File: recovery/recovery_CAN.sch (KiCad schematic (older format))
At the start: 15 parts, among them J1 Conn_01x05_Female, U1 MCP2562, U2 PIC18F26K83, Y1 Crystal

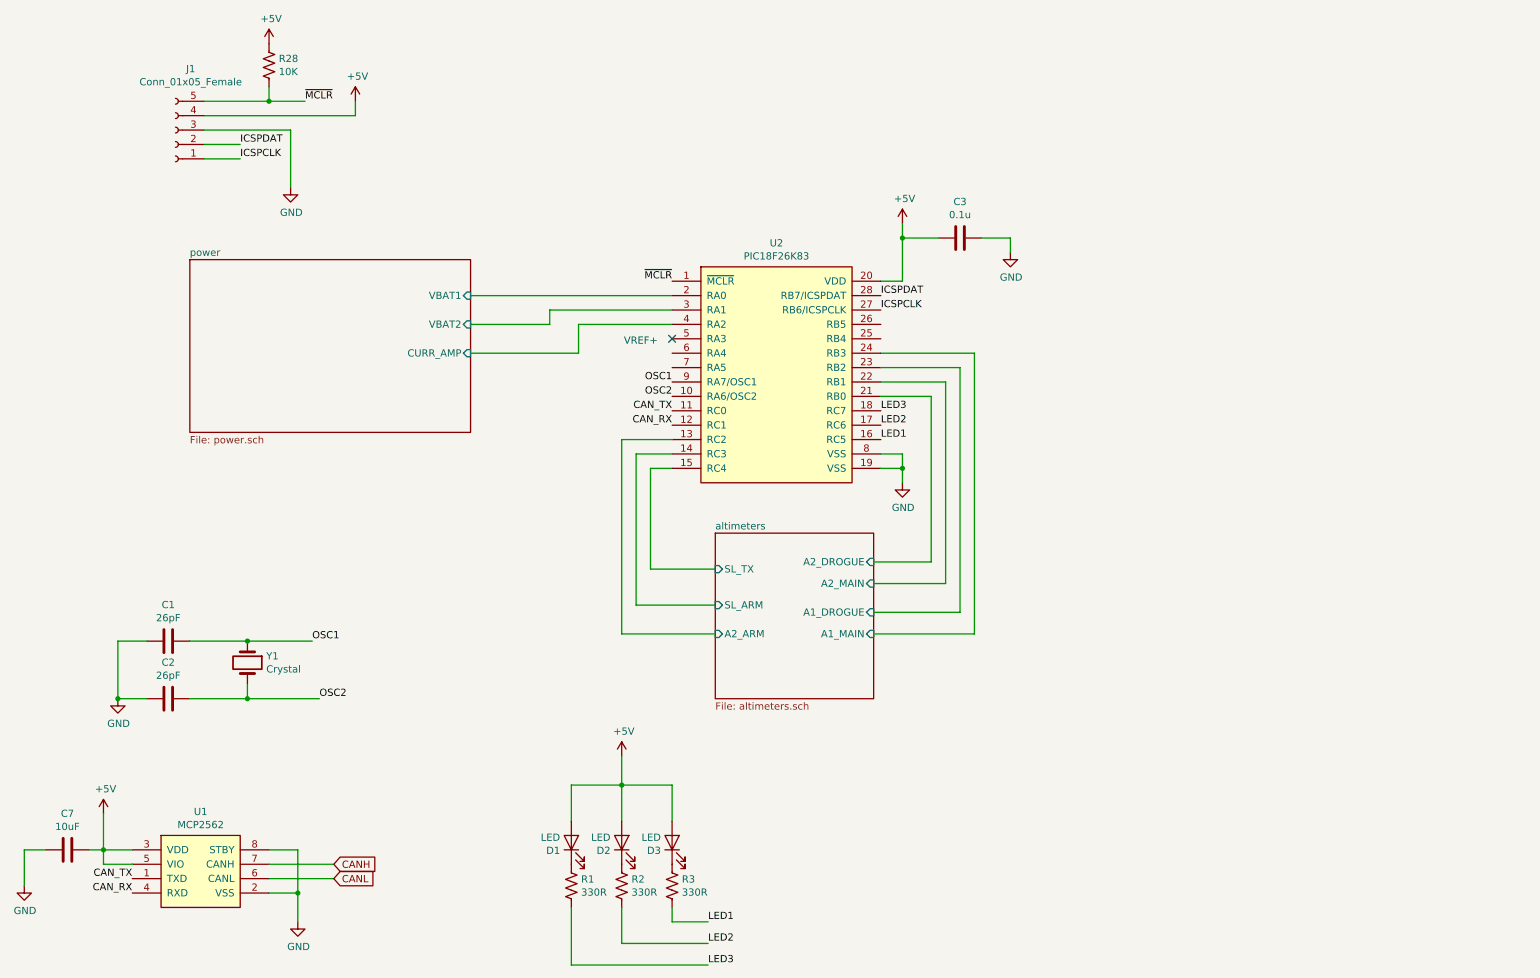
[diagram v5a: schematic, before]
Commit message: fix comments from scematic review, make mag switches powerup the PIC
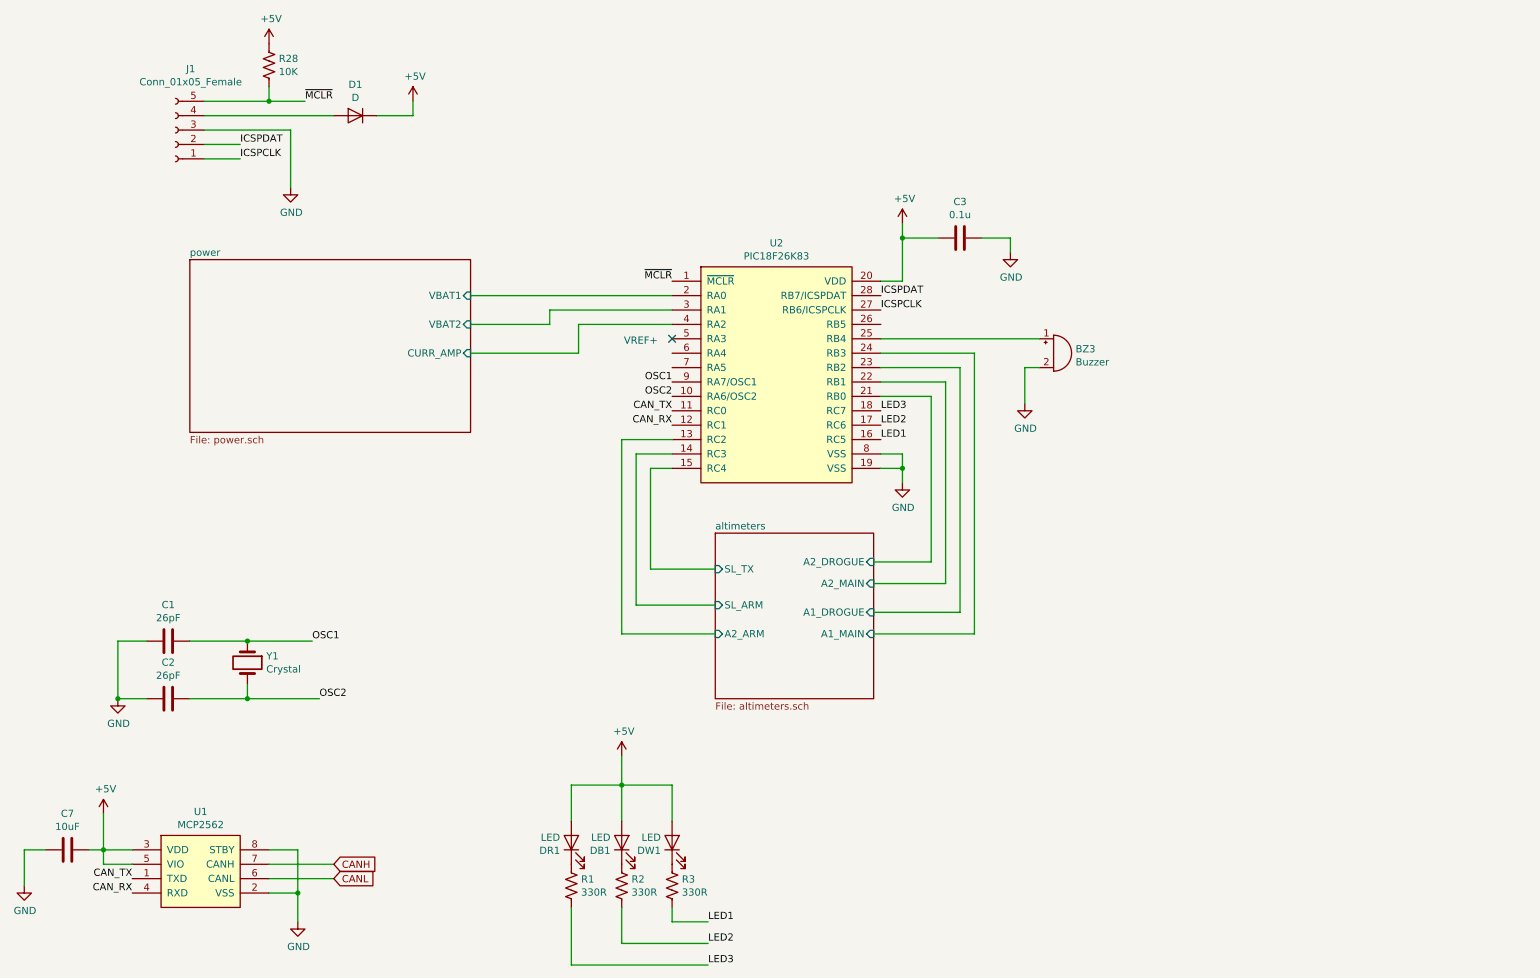
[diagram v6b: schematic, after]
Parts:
- added BZ3: Buzzer, symbol Device:Buzzer
- added D1: D, symbol Device:D
- renumbered D2 to DB1, D1 to DR1, D3 to DW1
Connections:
- net +5V: now also D1.1 (K); no longer J1.4 (Pin_4)
- net GND: now also BZ3.2 (+)
- net at U2.25 (RB4): now also BZ3.1 (-)
- new net: D1.2 (A), J1.4 (Pin_4)
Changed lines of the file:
@@
 L power:+5V #PWR03
 U 1 1 5D95A01E
-P 2950 1250
-F 0 "#PWR03" H 2950 1100 50  0001 C CNN
-F 1 "+5V" H 2965 1423 50  0000 C CNN
-F 2 "" H 2950 1250 50  0001 C CNN
-F 3 "" H 2950 1250 50  0001 C CNN
-	1    2950 1250
-	1    0    0    -1
-$EndComp
-Wire Wire Line
-	1900 1350 2950 1350
-Wire Wire Line
-	2950 1350 2950 1250
+P 3350 1250
+F 0 "#PWR03" H 3350 1100 50  0001 C CNN
+F 1 "+5V" H 3365 1423 50  0000 C CNN
+F 2 "" H 3350 1250 50  0001 C CNN
+F 3 "" H 3350 1250 50  0001 C CNN
+	1    3350 1250
+	1    0    0    -1
+$EndComp
+Wire Wire Line
+	1900 1350 2800 1350
 $Comp
 L power:GND #PWR04
@@
 $EndSheet
 $Comp
-L Device:LED D3
+L Device:LED DW1
 U 1 1 5DAA8959
 P 5150 6400
-F 0 "D3" V 5095 6478 50  0000 L CNN
+F 0 "DW1" V 5095 6478 50  0000 L CNN
 F 1 "LED" V 5186 6478 50  0000 L CNN
 F 2 "" H 5150 6400 50  0001 C CNN
@@
 $EndComp
 $Comp
-L Device:LED D2
+L Device:LED DB1
 U 1 1 5DAA89D1
 P 4800 6400
-F 0 "D2" V 4745 6478 50  0000 L CNN
+F 0 "DB1" V 4745 6478 50  0000 L CNN
 F 1 "LED" V 4836 6478 50  0000 L CNN
 F 2 "" H 4800 6400 50  0001 C CNN
@@
 $EndComp
 $Comp
-L Device:LED D1
+L Device:LED DR1
 U 1 1 5DAA8A2E
 P 4450 6400
-F 0 "D1" V 4395 6478 50  0000 L CNN
+F 0 "DR1" V 4395 6478 50  0000 L CNN
 F 1 "LED" V 4486 6478 50  0000 L CNN
 F 2 "" H 4450 6400 50  0001 C CNN
@@
 Wire Wire Line
 	1400 6550 1200 6550
-Wire Wire Line
-	1200 6200 1200 6450
 Connection ~ 1200 6450
 Wire Wire Line
@@
 	2200 5000 2650 5000
 Connection ~ 2200 5000
+Wire Wire Line
+	1200 6200 1200 6450
+$Comp
+L Device:D D1
+U 1 1 5DC3AC48
+P 2950 1350
+F 0 "D1" H 2950 1566 50  0000 C CNN
+F 1 "D" H 2950 1475 50  0000 C CNN
+F 2 "" H 2950 1350 50  0001 C CNN
+F 3 "~" H 2950 1350 50  0001 C CNN
+	1    2950 1350
+	-1   0    0    -1
+$EndComp
+Wire Wire Line
+	3350 1250 3350 1350
+Wire Wire Line
+	3350 1350 3100 1350
+$Comp
+L Device:Buzzer BZ3
+U 1 1 5DC989E9
+P 7800 3000
+F 0 "BZ3" H 7953 3029 50  0000 L CNN
+F 1 "Buzzer" H 7953 2938 50  0000 L CNN
+F 2 "" V 7775 3100 50  0001 C CNN
+F 3 "~" V 7775 3100 50  0001 C CNN
+	1    7800 3000
+	1    0    0    -1
+$EndComp
+Wire Wire Line
+	6600 2900 7700 2900
+$Comp
+L power:GND #PWR010
+U 1 1 5DC9A870
+P 7600 3350
+F 0 "#PWR010" H 7600 3100 50  0001 C CNN
+F 1 "GND" H 7605 3177 50  0000 C CNN
+F 2 "" H 7600 3350 50  0001 C CNN
+F 3 "" H 7600 3350 50  0001 C CNN
+	1    7600 3350
+	1    0    0    -1
+$EndComp
+Wire Wire Line
+	7700 3100 7600 3100
+Wire Wire Line
+	7600 3100 7600 3350
 $EndSCHEMATC

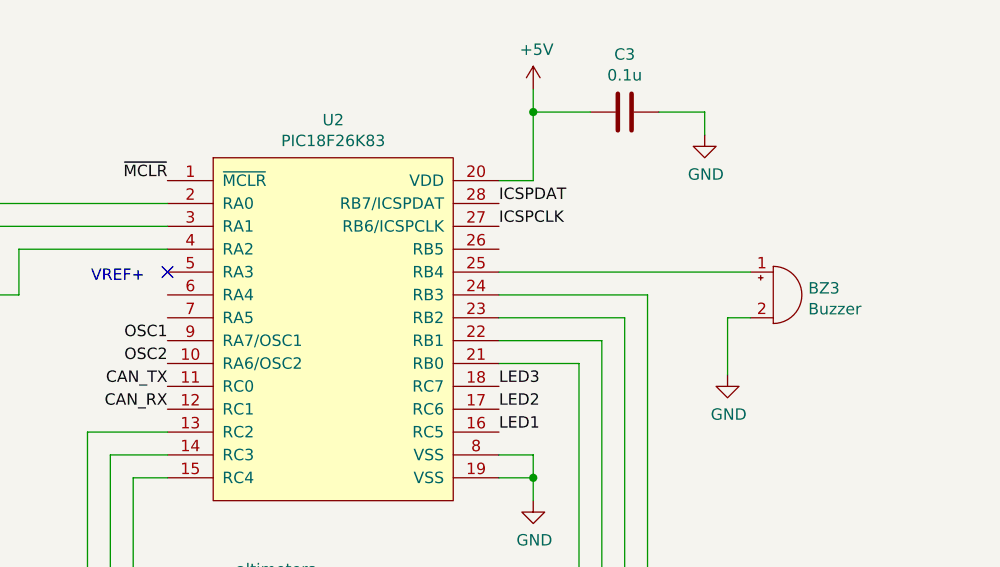
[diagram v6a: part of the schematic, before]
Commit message: add part numbers for buzzers
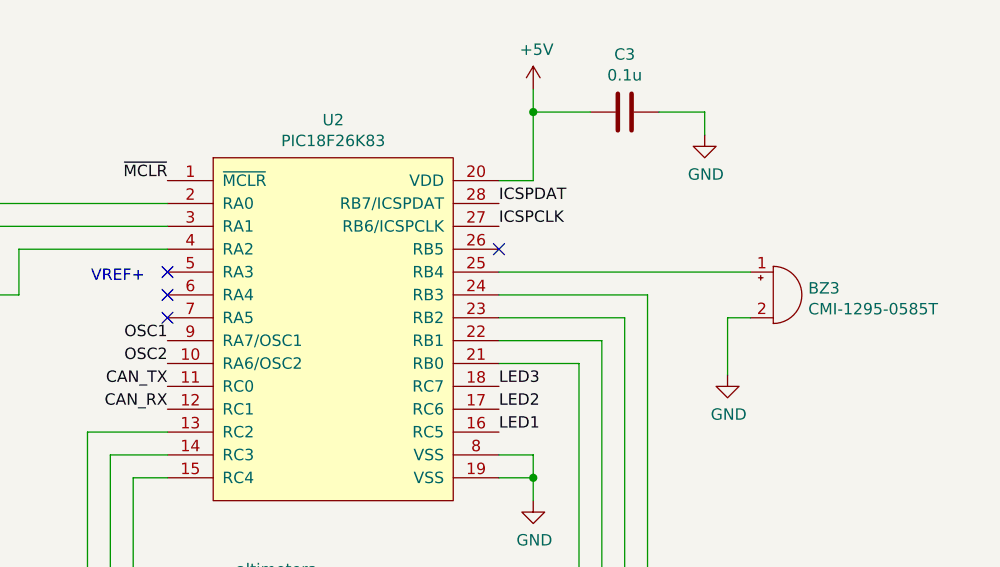
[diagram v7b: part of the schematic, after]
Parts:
- BZ3: value Buzzer -> CMI-1295-0585T
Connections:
- no-connect marks 1 -> 4
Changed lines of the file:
@@
 P 7800 3000
 F 0 "BZ3" H 7953 3029 50  0000 L CNN
-F 1 "Buzzer" H 7953 2938 50  0000 L CNN
+F 1 "CMI-1295-0585T" H 7953 2938 50  0000 L CNN
 F 2 "" V 7775 3100 50  0001 C CNN
 F 3 "~" V 7775 3100 50  0001 C CNN
@@
 Wire Wire Line
 	7600 3100 7600 3350
+NoConn ~ 6600 2800
+NoConn ~ 5150 3000
+NoConn ~ 5150 3100
 $EndSCHEMATC

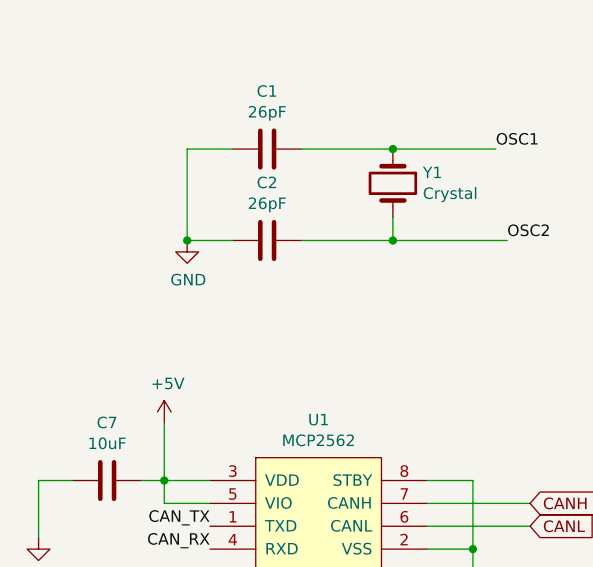
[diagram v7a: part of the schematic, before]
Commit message: Redesined scematic to reflect change to conectors for altimeter wiring, added more solder jumpers for increased board flexibility, created PCB file.
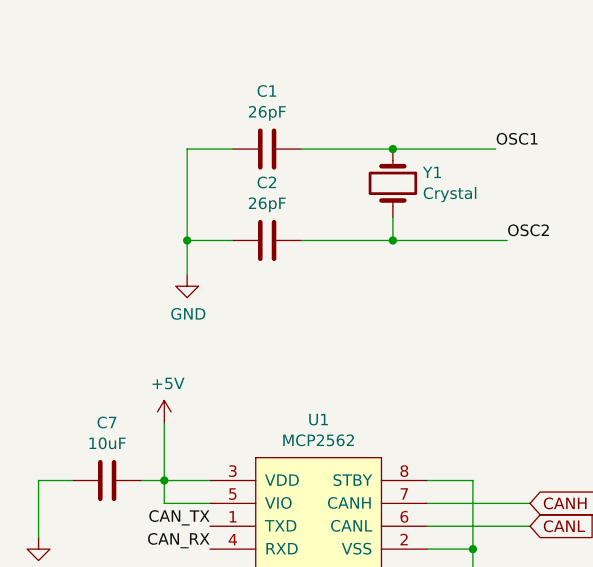
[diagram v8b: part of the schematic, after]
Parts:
- C1, C2, C3, C7: footprint (none) -> Capacitor_SMD:C_0805_2012Metric_Pad1.15x1.40mm_HandSolder
- DB1, DR1, DW1: footprint (none) -> LED_SMD:LED_1206_3216Metric_Pad1.42x1.75mm_HandSolder
- J1: footprint (none) -> canhw_footprints:PinHeader_5x2.54_SMD_90deg_952-3198-1-ND
- R1, R2, R28, R3: footprint (none) -> Resistor_SMD:R_0805_2012Metric_Pad1.15x1.40mm_HandSolder
- U1: footprint (none) -> Package_SO:SOIC-8_3.9x4.9mm_P1.27mm
- U2: footprint (none) -> Package_SO:SOIC-28W_7.5x18.7mm_P1.27mm
- Y1: footprint (none) -> Crystal:Crystal_HC49-4H_Vertical
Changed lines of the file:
@@
 F 0 "U2" H 5875 4065 50  0000 C CNN
 F 1 "PIC18F26K83" H 5875 3974 50  0000 C CNN
-F 2 "" H 6350 3150 50  0001 C CNN
+F 2 "Package_SO:SOIC-28W_7.5x18.7mm_P1.27mm" H 6350 3150 50  0001 C CNN
 F 3 "http://ww1.microchip.com/downloads/en/DeviceDoc/40001943A.pdf" H 6350 3150 50  0001 C CNN
 	1    5900 3150
@@
 F 0 "C3" V 6898 2200 50  0000 C CNN
 F 1 "0.1u" V 6989 2200 50  0000 C CNN
-F 2 "" H 7188 2050 50  0001 C CNN
+F 2 "Capacitor_SMD:C_0805_2012Metric_Pad1.15x1.40mm_HandSolder" H 7188 2050 50  0001 C CNN
 F 3 "~" H 7150 2200 50  0001 C CNN
 	1    7150 2200
@@
 F 0 "Y1" V 2154 5281 50  0000 L CNN
 F 1 "Crystal" V 2245 5281 50  0000 L CNN
-F 2 "" H 2200 5150 50  0001 C CNN
+F 2 "Crystal:Crystal_HC49-4H_Vertical" H 2200 5150 50  0001 C CNN
 F 3 "~" H 2200 5150 50  0001 C CNN
 	1    2200 5150
@@
 F 0 "C1" V 1398 5000 50  0000 C CNN
 F 1 "26pF" V 1489 5000 50  0000 C CNN
-F 2 "" H 1688 4850 50  0001 C CNN
+F 2 "Capacitor_SMD:C_0805_2012Metric_Pad1.15x1.40mm_HandSolder" H 1688 4850 50  0001 C CNN
 F 3 "~" H 1650 5000 50  0001 C CNN
 	1    1650 5000
@@
 F 0 "C2" V 1398 5400 50  0000 C CNN
 F 1 "26pF" V 1489 5400 50  0000 C CNN
-F 2 "" H 1688 5250 50  0001 C CNN
+F 2 "Capacitor_SMD:C_0805_2012Metric_Pad1.15x1.40mm_HandSolder" H 1688 5250 50  0001 C CNN
 F 3 "~" H 1650 5400 50  0001 C CNN
 	1    1650 5400
@@
 L power:GND #PWR02
 U 1 1 5D8FD7A1
-P 1300 5400
-F 0 "#PWR02" H 1300 5150 50  0001 C CNN
-F 1 "GND" H 1305 5227 50  0000 C CNN
-F 2 "" H 1300 5400 50  0001 C CNN
-F 3 "" H 1300 5400 50  0001 C CNN
-	1    1300 5400
-	1    0    0    -1
-$EndComp
-Wire Wire Line
-	1500 5400 1300 5400
+P 1300 5550
+F 0 "#PWR02" H 1300 5300 50  0001 C CNN
+F 1 "GND" H 1305 5377 50  0000 C CNN
+F 2 "" H 1300 5550 50  0001 C CNN
+F 3 "" H 1300 5550 50  0001 C CNN
+	1    1300 5550
+	1    0    0    -1
+$EndComp
 Wire Wire Line
 	1500 5000 1300 5000
-Wire Wire Line
-	1300 5000 1300 5400
-Connection ~ 1300 5400
 Wire Wire Line
 	1800 5000 2200 5000
@@
 F 0 "J1" H 1594 1025 50  0000 C CNN
 F 1 "Conn_01x05_Female" H 1594 1116 50  0000 C CNN
-F 2 "" H 1700 1450 50  0001 C CNN
+F 2 "canhw_footprints:PinHeader_5x2.54_SMD_90deg_952-3198-1-ND" H 1700 1450 50  0001 C CNN
 F 3 "~" H 1700 1450 50  0001 C CNN
 	1    1700 1450
@@
 F 0 "DW1" V 5095 6478 50  0000 L CNN
 F 1 "LED" V 5186 6478 50  0000 L CNN
-F 2 "" H 5150 6400 50  0001 C CNN
+F 2 "LED_SMD:LED_1206_3216Metric_Pad1.42x1.75mm_HandSolder" H 5150 6400 50  0001 C CNN
 F 3 "~" H 5150 6400 50  0001 C CNN
 	1    5150 6400
@@
 F 0 "DB1" V 4745 6478 50  0000 L CNN
 F 1 "LED" V 4836 6478 50  0000 L CNN
-F 2 "" H 4800 6400 50  0001 C CNN
+F 2 "LED_SMD:LED_1206_3216Metric_Pad1.42x1.75mm_HandSolder" H 4800 6400 50  0001 C CNN
 F 3 "~" H 4800 6400 50  0001 C CNN
 	1    4800 6400
@@
 F 0 "DR1" V 4395 6478 50  0000 L CNN
 F 1 "LED" V 4486 6478 50  0000 L CNN
-F 2 "" H 4450 6400 50  0001 C CNN
+F 2 "LED_SMD:LED_1206_3216Metric_Pad1.42x1.75mm_HandSolder" H 4450 6400 50  0001 C CNN
 F 3 "~" H 4450 6400 50  0001 C CNN
 	1    4450 6400
@@
 F 0 "R3" H 5218 6746 50  0000 L CNN
 F 1 "330R" H 5218 6655 50  0000 L CNN
-F 2 "" V 5190 6690 50  0001 C CNN
+F 2 "Resistor_SMD:R_0805_2012Metric_Pad1.15x1.40mm_HandSolder" V 5190 6690 50  0001 C CNN
 F 3 "~" H 5150 6700 50  0001 C CNN
 	1    5150 6700
@@
 F 0 "R2" H 4868 6746 50  0000 L CNN
 F 1 "330R" H 4868 6655 50  0000 L CNN
-F 2 "" V 4840 6690 50  0001 C CNN
+F 2 "Resistor_SMD:R_0805_2012Metric_Pad1.15x1.40mm_HandSolder" V 4840 6690 50  0001 C CNN
 F 3 "~" H 4800 6700 50  0001 C CNN
 	1    4800 6700
@@
 F 0 "R1" H 4518 6746 50  0000 L CNN
 F 1 "330R" H 4518 6655 50  0000 L CNN
-F 2 "" V 4490 6690 50  0001 C CNN
+F 2 "Resistor_SMD:R_0805_2012Metric_Pad1.15x1.40mm_HandSolder" V 4490 6690 50  0001 C CNN
 F 3 "~" H 4450 6700 50  0001 C CNN
 	1    4450 6700
@@
 F 0 "U1" H 1875 6715 50  0000 C CNN
 F 1 "MCP2562" H 1875 6624 50  0000 C CNN
-F 2 "" H 1900 6450 50  0001 C CNN
+F 2 "Package_SO:SOIC-8_3.9x4.9mm_P1.27mm" H 1900 6450 50  0001 C CNN
 F 3 "http://hades.mech.northwestern.edu/images/5/5e/MCP2562.pdf" H 1900 6450 50  0001 C CNN
 	1    1900 6450
@@
 F 0 "R28" H 2418 1046 50  0000 L CNN
 F 1 "10K" H 2418 955 50  0000 L CNN
-F 2 "" V 2390 990 50  0001 C CNN
+F 2 "Resistor_SMD:R_0805_2012Metric_Pad1.15x1.40mm_HandSolder" V 2390 990 50  0001 C CNN
 F 3 "~" H 2350 1000 50  0001 C CNN
 	1    2350 1000
@@
 F 0 "C7" V 698 6450 50  0000 C CNN
 F 1 "10uF" V 789 6450 50  0000 C CNN
-F 2 "" H 988 6300 50  0001 C CNN
+F 2 "Capacitor_SMD:C_0805_2012Metric_Pad1.15x1.40mm_HandSolder" H 988 6300 50  0001 C CNN
 F 3 "~" H 950 6450 50  0001 C CNN
 	1    950  6450
@@
 NoConn ~ 5150 3000
 NoConn ~ 5150 3100
+Wire Wire Line
+	1300 5000 1300 5400
+Wire Wire Line
+	1500 5400 1300 5400
+Connection ~ 1300 5400
+Wire Wire Line
+	1300 5400 1300 5550
 $EndSCHEMATC
